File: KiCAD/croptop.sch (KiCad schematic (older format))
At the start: 0 parts

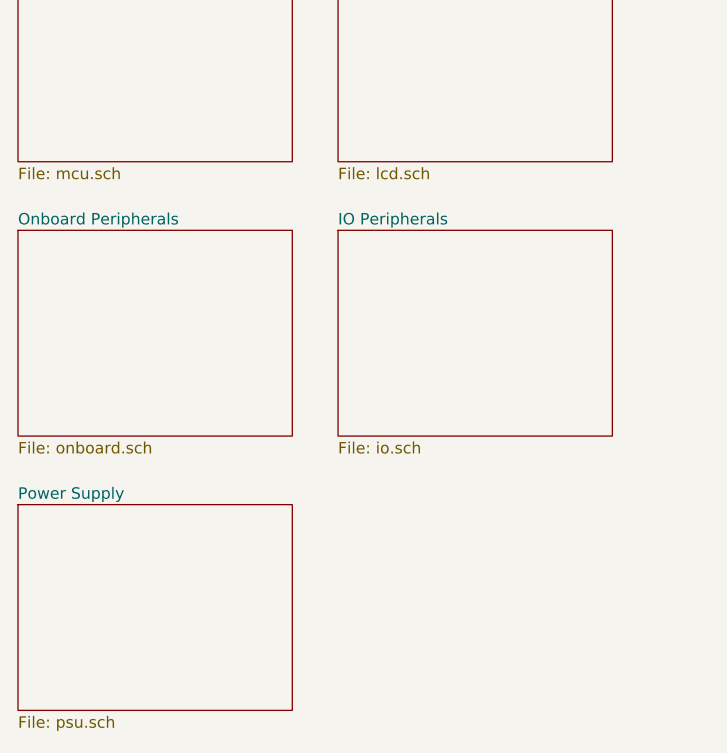
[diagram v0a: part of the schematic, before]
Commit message: Updates ESD protection diodes
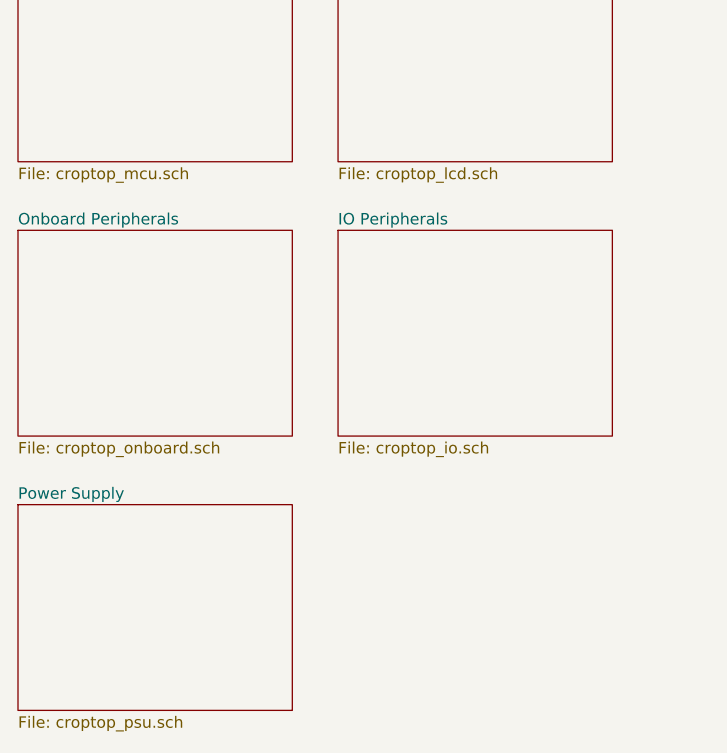
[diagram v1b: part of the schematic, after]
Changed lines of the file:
@@
 EESchema Schematic File Version 4
-LIBS:croptop_rev1-cache
+LIBS:croptop-cache
 EELAYER 26 0
 EELAYER END
@@
 U 64807BBC
 F0 "Microcontroller" 50
-F1 "mcu.sch" 50
+F1 "croptop_mcu.sch" 50
 $EndSheet
 $Sheet
@@
 U 64809F0C
 F0 "Power Supply" 50
-F1 "psu.sch" 50
+F1 "croptop_psu.sch" 50
 $EndSheet
 $Sheet
@@
 U 65B709D0
 F0 "Display" 50
-F1 "lcd.sch" 50
+F1 "croptop_lcd.sch" 50
 $EndSheet
 $Sheet
@@
 U 669AB112
 F0 "IO Peripherals" 50
-F1 "io.sch" 50
+F1 "croptop_io.sch" 50
 $EndSheet
 $Sheet
@@
 U 66A12230
 F0 "Onboard Peripherals" 50
-F1 "onboard.sch" 50
+F1 "croptop_onboard.sch" 50
 $EndSheet
 Text Notes 4100 1750 0    138  ~ 28

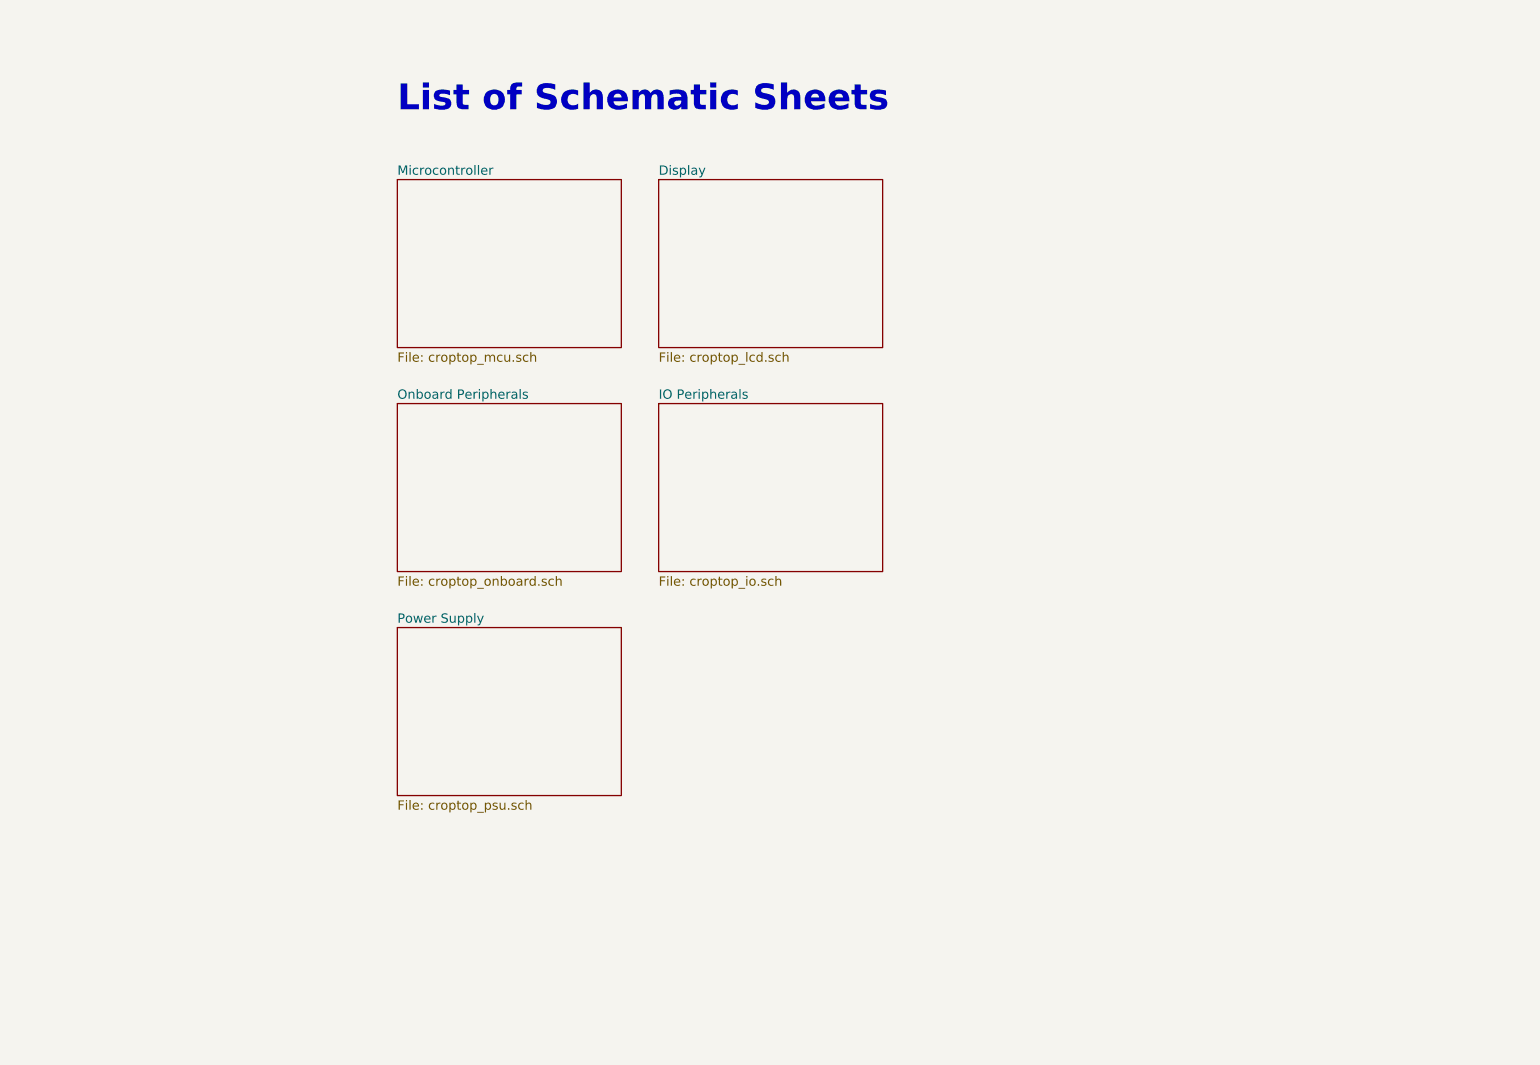
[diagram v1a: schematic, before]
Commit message: Got to PCB layout
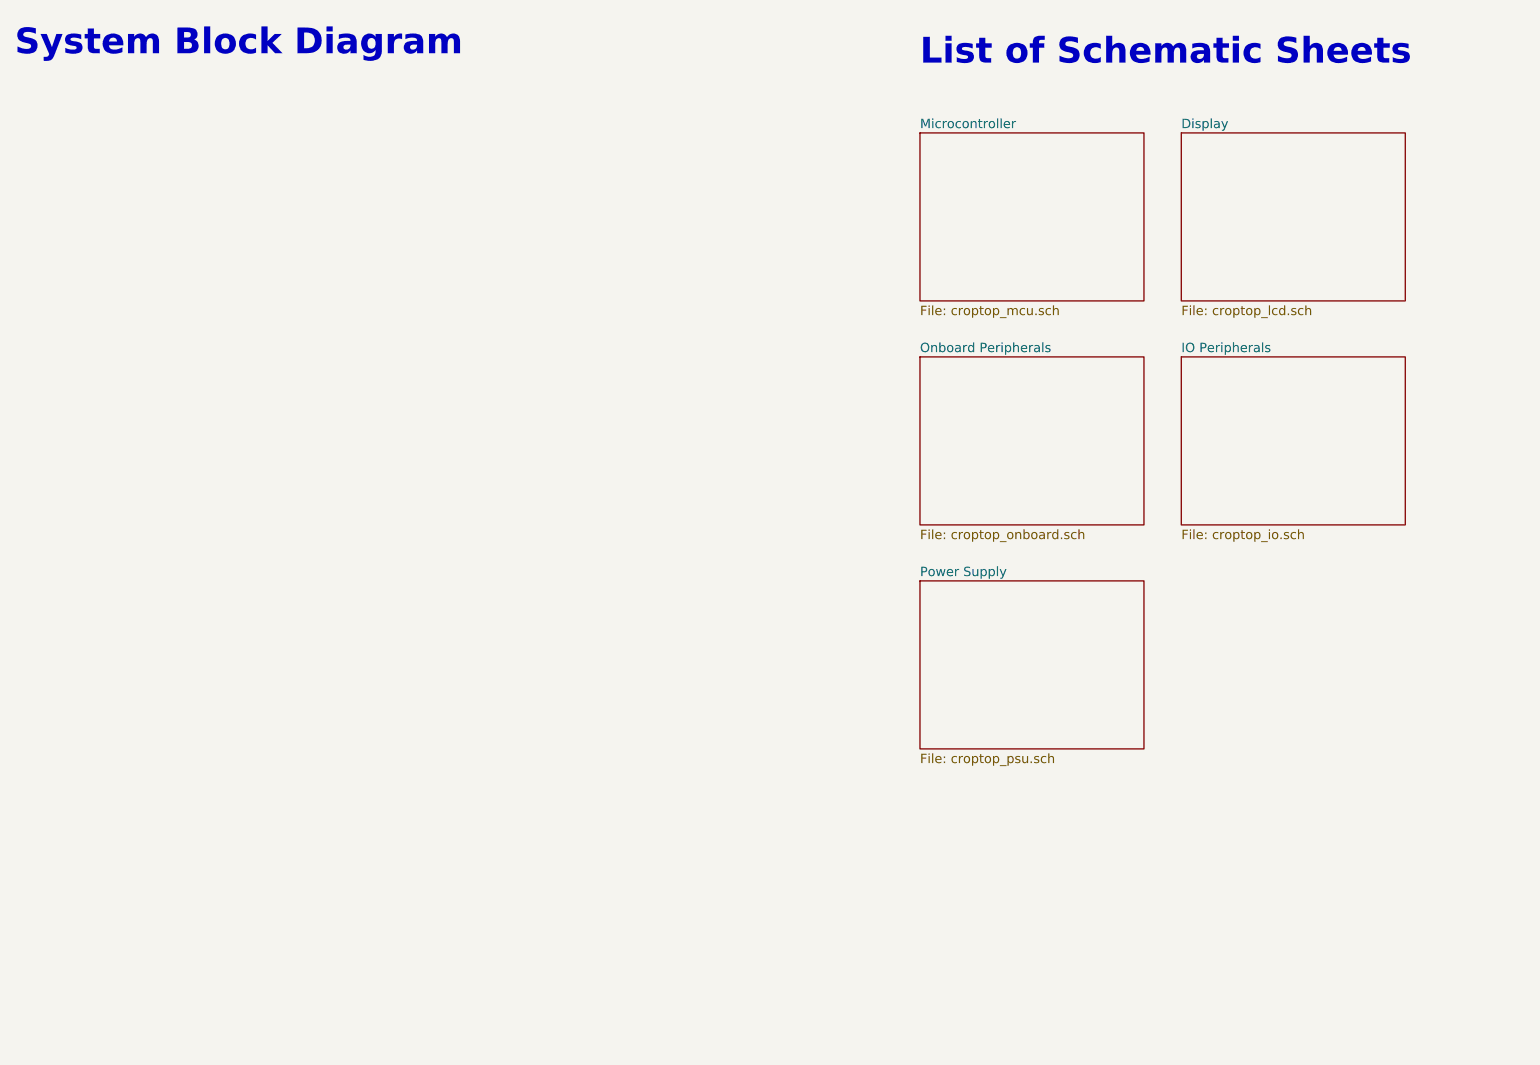
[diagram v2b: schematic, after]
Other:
- note added: "System Block Diagram"

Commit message: Adding images
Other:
- note added: "Change nets to have directions\nRemove global nets on power\nAdd missing pullups and pulldowns on temp/memory\nSpace out componentts more, use a bigger board\nConsider 0603 resistors/caps\nCheck regulators can carry high current\nMove far end of\nMove micro usb and lcd connector further forward"
- note added: "List of things to do:\nRemove electrolytic input on DC motor driver\nChange AVDD to 5V0_REG, DVDD to 3V3"
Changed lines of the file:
@@
 EndData
 $EndBitmap
+Text Notes 7350 6100 0    50   ~ 0
+List of things to do:\nRemove electrolytic input on DC motor driver\nChange AVDD to 5V0_REG, DVDD to 3V3
+Text Notes 7350 6750 0    50   ~ 0
+Change nets to have directions\nRemove global nets on power\nAdd missing pullups and pulldowns on temp/memory\nSpace out componentts more, use a bigger board\nConsider 0603 resistors/caps\nCheck regulators can carry high current\nMove far end of\nMove micro usb and lcd connector further forward
 $EndSCHEMATC

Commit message: Getting example files
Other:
- note added: "List of things to do:\nRemove electrolytic input on DC motor driver\nChange AVDD to 5V0_REG, DVDD to 3V3\nChange nets to have directions\nRemove global nets on power\nAdd missing pullups and pulldowns on temp/memory\nAdd MISO to SPI bus\nAdd resistor to Load bank for current limit\nMake board larger at top, add header blocks\nList of things to do:\nRemove electrolytic input on DC motor driver\nCh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"
- note removed: "Change nets to have directions\nRemove global nets on power\nAdd missing pullups and pulldowns on temp/memory\nSpace out componentts more, use a bigger board\nConsider 0603 resistors/caps\nCheck regulators can carry high current\nMove far end of\nMove micro usb and lcd connector further forward"
- note removed: "List of things to do:\nRemove electrolytic input on DC motor driver\nChange AVDD to 5V0_REG, DVDD to 3V3"
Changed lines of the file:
@@
 EndData
 $EndBitmap
-Text Notes 7350 6100 0    50   ~ 0
-List of things to do:\nRemove electrolytic input on DC motor driver\nChange AVDD to 5V0_REG, DVDD to 3V3
 Text Notes 7350 6750 0    50   ~ 0
-Change nets to have directions\nRemove global nets on power\nAdd missing pullups and pulldowns on temp/memory\nSpace out componentts more, use a bigger board\nConsider 0603 resistors/caps\nCheck regulators can carry high current\nMove far end of\nMove micro usb and lcd connector further forward
+List of things to do:\nRemove electrolytic input on DC motor driver\nChange AVDD to 5V0_REG, DVDD to 3V3\nChange nets to have directions\nRemove global nets on power\nAdd missing pullups and pulldowns on temp/memory\nAdd MISO to SPI bus\nAdd resistor to Load bank for current limit\nMake board larger at top, add header blocks\nList of things to do:\nRemove electrolytic input on DC motor driver\nChange AVDD to 5V0_REG, DVDD to 3V3\nCheck regulators can carry high current\nMove micro usb and lcd connector further forward
 $EndSCHEMATC
